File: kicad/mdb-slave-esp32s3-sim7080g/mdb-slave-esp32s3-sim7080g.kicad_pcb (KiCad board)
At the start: 2 copper layers, 65 x 40 mm, 69 parts, among them J1 USB_C_Receptacle_USB2.0_16P, J2 JAE_SIM_Card_SF72S006, J3 Conn_02x11_Odd_Even, J4 Conn_Coaxial, J5 Conn_Coaxial, J6 MDB_Connector, Q1 NPN, Q2 NPN, Q3 NPN, SW1 SW_Push, U1 ESP32-S3FH4R2, U2 SIM7080G, U3 LM2594HVM-3.3, U4 TLP785, U5 TLP785, Y1 Crystal_GND24

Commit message: Updating routes
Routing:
- net GND: track 425.9 -> 426.8 mm
- net /mdb_communications_common: track 30.1 -> 30.6 mm

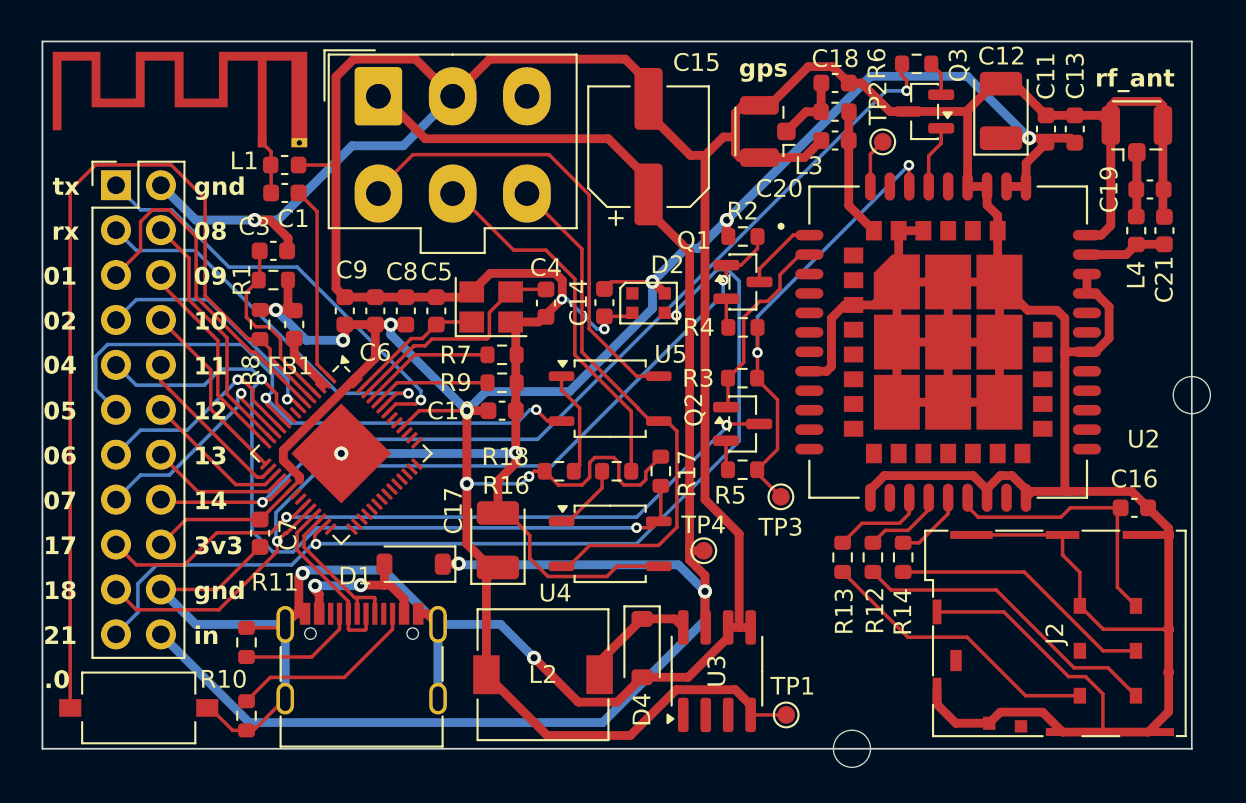
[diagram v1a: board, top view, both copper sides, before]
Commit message: Adding NTC thermal sensor
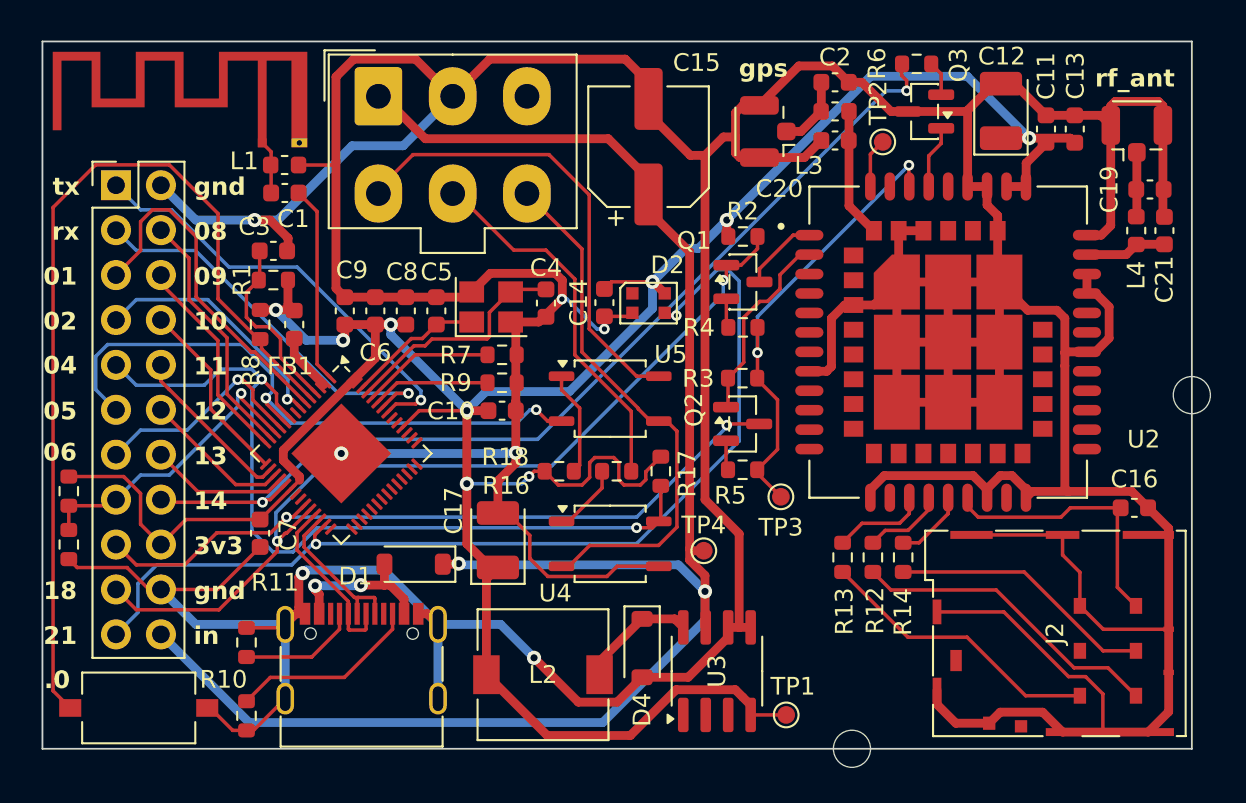
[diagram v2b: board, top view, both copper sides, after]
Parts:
- removed C18: 27pf, Capacitor_SMD:C_0603_1608Metric
- added C2: 1.8pf, Capacitor_SMD:C_0603_1608Metric, F.Cu at (213.3, 85.4)
- added R15: 10k, Resistor_SMD:R_0603_1608Metric, F.Cu at (170.0, 108.5)
- added TH1: Thermistor_NTC, Resistor_SMD:R_0603_1608Metric, F.Cu at (170.0, 111.5)
- C19: value 27pf -> 1.8pf
- L3: value 47nh -> 5.6nh
- L4: value 47nh -> 3.9nh
- R2, R3: value 10K -> 10k
- moved REF** 2.96 mm to (220.8, 111.5)
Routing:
- net +3V3: track 152.4 -> 160.3 mm
- net GND: track 426.8 -> 432.8 mm
- net /io7: track 12.9 -> 17.1 mm

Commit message: Updating LED footprint
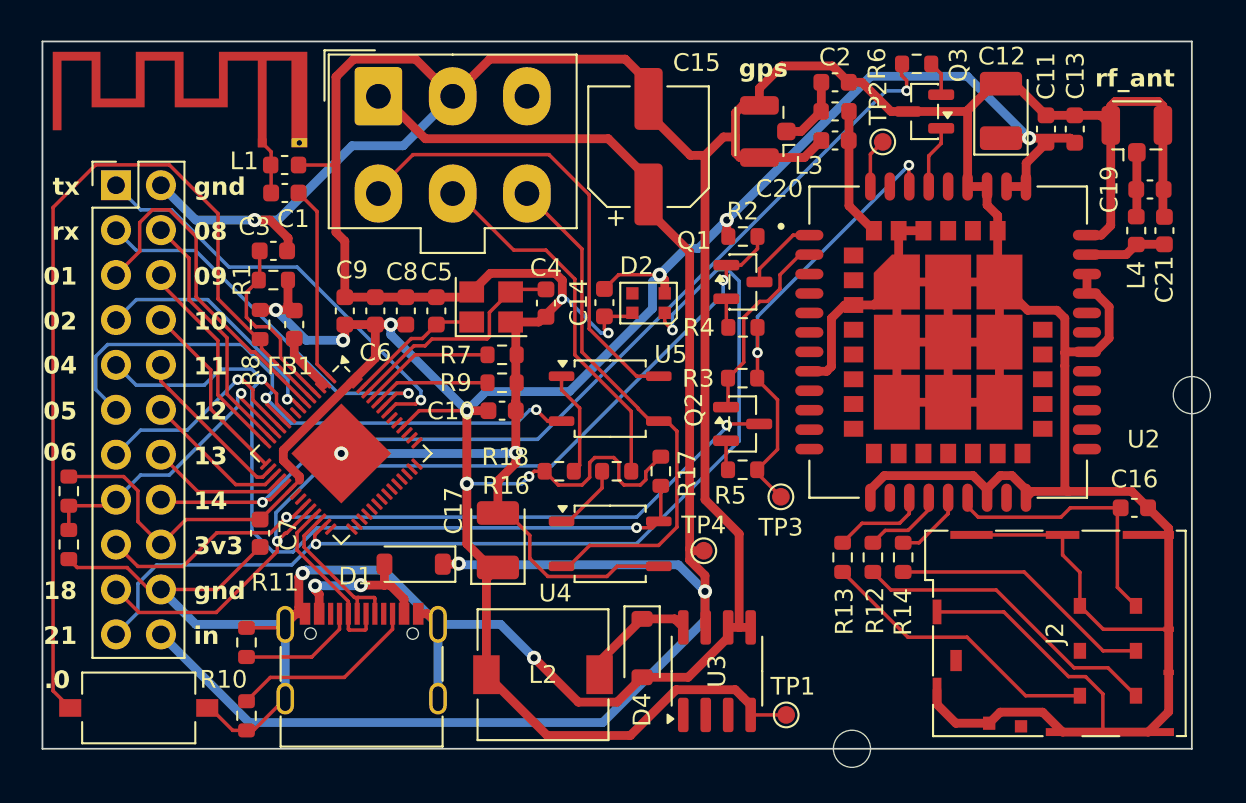
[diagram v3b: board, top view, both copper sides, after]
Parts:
- moved REF** 5.61 mm to (221.5, 106.0)
- turned D2 to 180 degrees
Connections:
- D2 pad 1: unconnected-(D2-DOUT-Pad1) -> /io21
- D2 pad 2: GND -> +3V3
- D2 pad 3: /io21 -> unconnected-(D2-DOUT-Pad3)
- D2 pad 4: +3V3 -> GND
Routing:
- net /io21: track 57.0 -> 58.3 mm
- net GND: track 432.8 -> 434.0 mm
- net +3V3: track 160.3 -> 161.1 mm

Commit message: Updating sim7080g transistors
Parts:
- removed REF**: OSHW-Logo2_14.6x12mm_SilkScreen, Symbol:OSHW-Logo2_14.6x12mm_SilkScreen
- Q1, Q2, Q3: value NPN -> MMBT3904
- moved Q2 21.4 mm to (218.5, 86.1), turned to 180 degrees
- moved Q3 14.1 mm to (208.1, 96.7)
- moved Q1 8.09 mm to (208.1, 104.8), turned to 180 degrees
- moved R6 4.54 mm to (218.9, 88.8)
- moved TP2 0.89 mm to (216.0, 87.9)
- moved R4 0.12 mm to (208.1, 99.4)
- moved C20 0.10 mm to (213.3, 88.8)
- moved L3 0.05 mm to (213.3, 87.1)
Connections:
- Q1 pad 1: /io18 -> Net-(Q1-B)
- Q1 pad 2: Net-(Q1-B) -> /io17
- Q1 pad 3: /sim_uart1_tx -> /sim_uart1_rx
- Q2 pad 1: /sim_uart1_rx -> Net-(Q2-B)
- Q2 pad 2: Net-(Q2-B) -> GND
- Q2 pad 3: /io17 -> /pwrkey
- Q3 pad 1: /pwrkey -> Net-(Q3-B)
- Q3 pad 2: Net-(Q3-B) -> /sim_uart1_tx
- Q3 pad 3: GND -> /io18
- R4 pad 2: Net-(Q1-B) -> Net-(Q3-B)
- R5 pad 2: Net-(Q2-B) -> Net-(Q1-B)
- R6 pad 1: Net-(Q3-B) -> Net-(Q2-B)
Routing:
- net /pwrkey: track 3.58 -> 5.76 mm
- net /io14: track 55.3 -> 53.1 mm
- net /sim_uart1_rx: track 11.1 -> 12.6 mm
- net Net-(Q1-B): track 1.67 -> 2.79 mm
- net Net-(Q3-B): track 1.97 -> 3.00 mm
- net Net-(U2-STATUS): track 2.81 -> 3.70 mm
- net /io17: track 41.7 -> 42.3 mm
- net /io18: track 51.0 -> 50.4 mm
- net /sim_uart1_tx: track 4.35 -> 3.76 mm

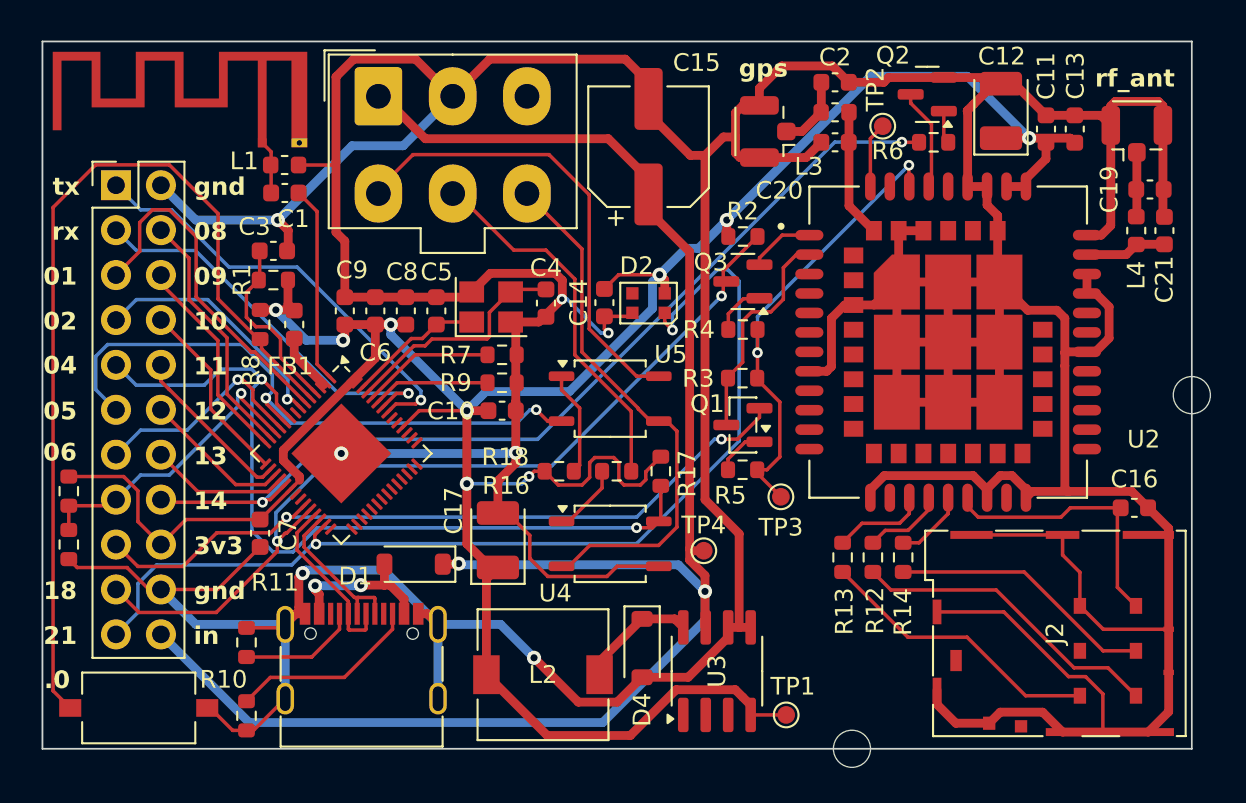
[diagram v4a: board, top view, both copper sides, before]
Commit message: Adding buzzer and DEX level shifter
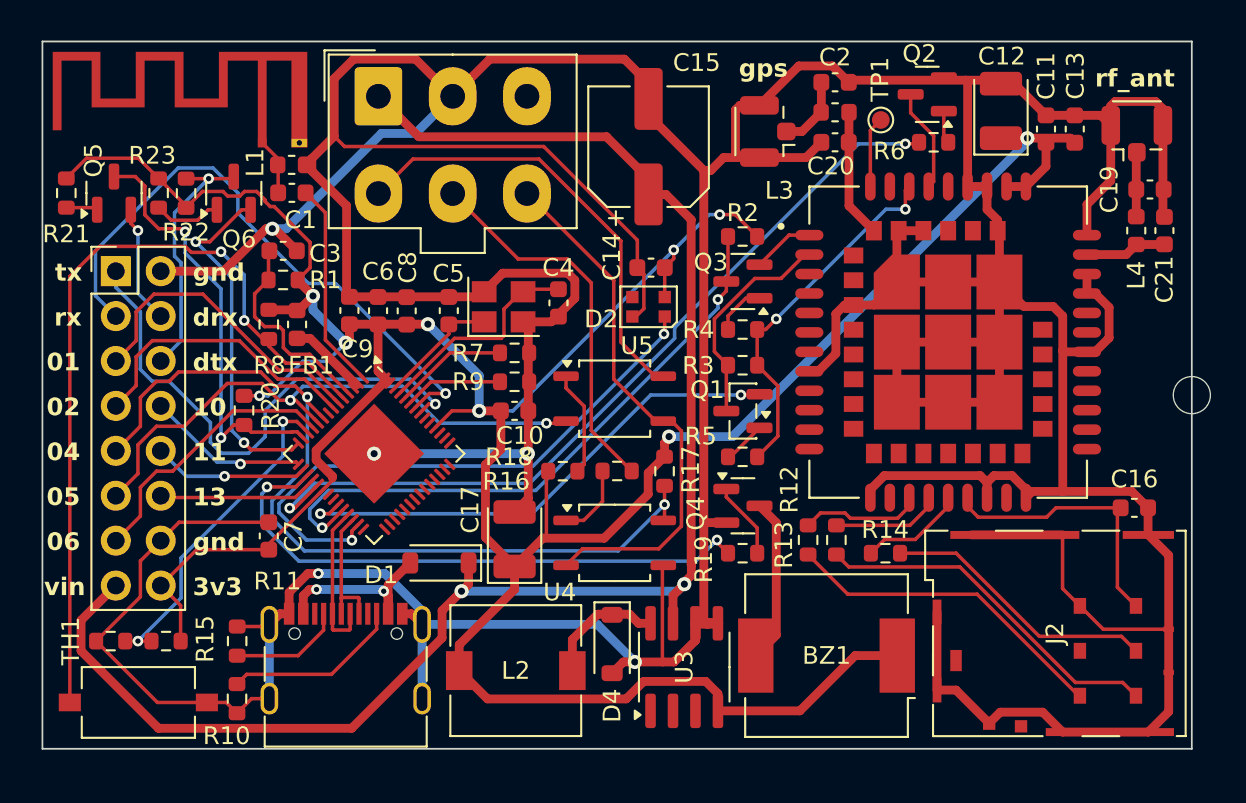
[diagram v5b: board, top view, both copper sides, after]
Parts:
- removed H2: MountingHole, MountingHole:MountingHole_2.1mm
- removed J3: Conn_02x11_Odd_Even, Connector_PinHeader_2.54mm:PinHeader_2x11_P2.54mm_Vertical
- removed TP2, TP3, TP4: TestPoint, TestPoint:TestPoint_Pad_D1.0mm
- added BZ1: Buzzer, Buzzer_Beeper:Buzzer_CUI_CPT-9019S-SMT, F.Cu at (212.8, 117.8)
- added J7: Conn_02x08_Odd_Even, Connector_PinHeader_2.54mm:PinHeader_2x08_P2.54mm_Vertical, F.Cu at (172.7, 96.1)
- added Q4: MMBT3904, Package_TO_SOT_SMD:SOT-23, F.Cu at (208.1, 109.3)
- added Q5: MMBT3904, Package_TO_SOT_SMD:SOT-23, F.Cu at (172.5, 91.7)
- added Q6: MMBT3904, Package_TO_SOT_SMD:SOT-23, F.Cu at (179.3, 91.7)
- added R19: 4K7, Resistor_SMD:R_0603_1608Metric, F.Cu at (208.1, 112.0)
- added R20: 10k, Resistor_SMD:R_0603_1608Metric, F.Cu at (179.9, 104.0)
- added R21: 4K7, Resistor_SMD:R_0603_1608Metric, F.Cu at (169.8, 91.7)
- added R22: 10k, Resistor_SMD:R_0603_1608Metric, F.Cu at (176.6, 91.7)
- added R23: 4K7, Resistor_SMD:R_0603_1608Metric, F.Cu at (175.1, 91.7)
- added REF**: OSHW-Logo_11.4x12mm_SilkScreen, Symbol:OSHW-Logo_11.4x12mm_SilkScreen, B.Cu at (220.7, 104.4)
- moved TP1 34.1 mm to (215.9, 87.5)
- moved H1 27.7 mm to (233.5, 103.1)
- moved R15 10.1 mm to (175.5, 117.0), turned to 0 degrees
- moved TH1 5.95 mm to (172.4, 117.0), turned to 0 degrees
- moved C14 3.30 mm to (202.9, 95.9), turned to 0 degrees
- moved R12 2.29 mm to (213.4, 111.3)
- moved R13 2.18 mm to (211.8, 111.3)
- moved U3 1.86 mm to (204.8, 118.5)
- moved U1 1.85 mm to (187.3, 106.4)
- moved D4 1.71 mm to (200.7, 117.2)
- moved L2 1.56 mm to (195.3, 118.7)
- moved D1 1.46 mm to (190.9, 112.6)
- moved R10 1.11 mm to (179.5, 120.3)
- moved R14 1.03 mm to (216.2, 112.0), turned to 0 degrees
- moved C17 0.94 mm to (195.2, 111.2)
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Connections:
- C10 pad 1: GND -> +3V3
- C10 pad 2: +3V3 -> GND
- C9 pad 1: GND -> +3V3
- C9 pad 2: +3V3 -> GND
- TP1 pad 1: +3V3 -> Net-(U2-STATUS)
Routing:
- net +3V3: track 161.1 -> 199.1 mm
- net /io21: track 58.3 -> 33.1 mm
- net /io12: track 8.49 -> 33.0 mm, vias 0 -> 2
- net /io18: track 50.4 -> 35.2 mm
- net /dex_tx: track 0.00 -> 14.5 mm, vias 0 -> 1
- net /io17: track 42.3 -> 28.9 mm
- net GND: track 434.4 -> 422.0 mm, vias 7 -> 5
- net /u0rxd: track 22.2 -> 33.9 mm
- net /io8: track 14.3 -> 24.0 mm, vias 0 -> 2
- net Net-(BZ1--): track 0.00 -> 9.34 mm
- net /io9: track 11.9 -> 19.7 mm, vias 0 -> 2
- net /boot: track 52.8 -> 45.6 mm, vias 0 -> 2
- net /dex_rx: track 0.00 -> 6.72 mm, vias 0 -> 1
- net /io14: track 53.1 -> 46.7 mm
- net /vin: track 97.2 -> 90.8 mm
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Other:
- board text added: "drx"
- board text added: "dtx"
- board text added: "vin"
- board text removed: ".0"
- board text removed: "07"
- board text removed: "08"
- board text removed: "09"
- board text removed: "12"
- board text removed: "14"
- board text removed: "17"
- board text removed: "18"
- board text removed: "21"
- board text removed: "in"

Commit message: routing..
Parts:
- removed REF**: OSHW-Logo_11.4x12mm_SilkScreen, Symbol:OSHW-Logo_11.4x12mm_SilkScreen
- added J3: Conn_01x03_Pin, Connector_JST:JST_PH_B3B-PH-K_1x03_P2.00mm_Vertical, F.Cu at (175.9, 93.1)
- added J8: Conn_01x04_Pin, Connector_JST:JST_PH_B4B-PH-K_1x04_P2.00mm_Vertical, F.Cu at (177.9, 103.5)
- added Q7: MMBT3904, Package_TO_SOT_SMD:SOT-23, F.Cu at (172.4, 115.9)
- added R24: 4K7, Resistor_SMD:R_0603_1608Metric, F.Cu at (174.1, 106.9)
- added R25: 4K7, Resistor_SMD:R_0603_1608Metric, F.Cu at (171.0, 106.9)
- added R27: 4K7, Resistor_SMD:R_0603_1608Metric, F.Cu at (175.4, 115.9)
- J7: value Conn_02x08_Odd_Even -> Conn_01x03_Pin; footprint Connector_PinHeader_2.54mm:PinHeader_2x08_P2.54mm_Vertical -> Connector_JST:JST_PH_B3B-PH-K_1x03_P2.00mm_Vertical
- moved J7 15.8 mm to (175.9, 111.5), turned to 180 degrees
- moved R21 12.2 mm to (180.1, 98.3)
- moved Q6 10.6 mm to (170.6, 97.7)
- moved R15 9.02 mm to (179.5, 108.9), turned to 90 degrees
- moved TH1 8.59 mm to (179.5, 112.2), turned to 90 degrees
- moved Q5 7.92 mm to (177.5, 97.8)
- moved R23 6.88 mm to (173.2, 98.3)
- moved R22 6.86 mm to (174.8, 98.3)
- moved R20 1.74 mm to (181.6, 103.7)
- moved C7 1.23 mm to (181.6, 112.2)
- moved C9 1.01 mm to (184.8, 98.3)
- moved C3 0.93 mm to (182.5, 94.1)
- moved R1 0.93 mm to (182.5, 95.7)
- moved R8 0.86 mm to (181.7, 98.3)
- moved FB1 0.86 mm to (183.3, 98.3)
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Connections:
- J7 pad 1: /u0txd -> GND
- J7 pad 2: GND -> /vin
- J7 pad 3: /u0rxd -> Net-(J7-Pin_3)
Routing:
- net GND: track 422.0 -> 0.00 mm, vias 5 -> 0
- net +3V3: track 199.1 -> 0.00 mm, vias 9 -> 0
- net /vin: track 90.8 -> 0.00 mm, vias 2 -> 0
- net /io4: track 49.5 -> 0.00 mm, vias 2 -> 0
- net /io14: track 46.7 -> 0.00 mm, vias 2 -> 0
- net /boot: track 45.6 -> 0.00 mm, vias 2 -> 0
- net /io18: track 35.2 -> 0.00 mm, vias 2 -> 0
- net /u0rxd: track 33.9 -> 0.00 mm, vias 1 -> 0
- net /io21: track 33.1 -> 0.00 mm, vias 2 -> 0
- net /io12: track 33.0 -> 0.00 mm, vias 2 -> 0
- net /io5: track 32.8 -> 0.00 mm, vias 2 -> 0
- net /mdb_communications_common: track 30.4 -> 0.00 mm
- net /u0txd: track 29.7 -> 0.00 mm, vias 1 -> 0
- net /io17: track 28.9 -> 0.00 mm, vias 2 -> 0
- net /mdb_master_receive: track 25.4 -> 0.00 mm
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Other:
- board text removed: "01"
- board text removed: "02"
- board text removed: "04"
- board text removed: "05"
- board text removed: "06"
- board text removed: "10"
- board text removed: "11"
- board text removed: "13"
- board text removed: "3v3"
- board text removed: "drx"
- board text removed: "dtx"
- board text removed: "gnd"
- board text removed: "rx"
- board text removed: "tx"
- board text removed: "vin"

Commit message: routing...
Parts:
- moved C8 0.30 mm to (189.4, 98.3)
- moved C6 0.30 mm to (187.8, 98.3)
- moved R7 0.14 mm to (195.2, 100.8)
- moved Q5 0.11 mm to (177.4, 97.8), turned to -90 degrees
- moved R9 0.07 mm to (195.2, 102.4)
- moved Q6 0.06 mm to (170.7, 97.7)
- moved C9 0.06 mm to (184.9, 98.3)
- moved FB1 0.06 mm to (183.3, 98.3)
- moved R21 0.06 mm to (180.1, 98.3)
- moved R22 0.06 mm to (174.8, 98.3)
- moved R23 0.06 mm to (173.3, 98.3), turned to 90 degrees
- moved R8 0.06 mm to (181.7, 98.3)
- turned C7 to 90 degrees
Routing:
- net /boot: track 0.00 -> 51.3 mm
- net +3V3: track 0.00 -> 50.4 mm
- net GND: track 0.00 -> 46.2 mm, vias 0 -> 1
- net /io11: track 0.00 -> 19.0 mm
- net /io9: track 0.00 -> 15.5 mm
- net Net-(U1-CHIP_PU/RESET): track 0.00 -> 14.4 mm
- net /io10: track 0.00 -> 14.2 mm
- net /io13: track 0.00 -> 12.0 mm
- net Net-(U1-XTAL_N): track 0.00 -> 12.0 mm
- net Net-(J1-CC2): track 0.00 -> 10.0 mm
- net /dex_tx: track 0.00 -> 9.81 mm
- net /io8: track 0.00 -> 9.71 mm
- net /usb-: track 0.00 -> 9.09 mm
- net /usb+: track 0.00 -> 8.71 mm
- net Net-(D1-A): track 0.00 -> 7.41 mm, vias 0 -> 2
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
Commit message: routing...
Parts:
- added REF**: OSHW-Logo_11.4x12mm_SilkScreen, Symbol:OSHW-Logo_11.4x12mm_SilkScreen, B.Cu at (210.5, 109.1)
- moved C11 0.40 mm to (224.9, 88.0)
- moved C12 0.40 mm to (222.3, 87.0)
- moved C13 0.40 mm to (226.5, 88.0)
- turned R18 to 180 degrees
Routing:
- net GND: track 46.2 -> 427.7 mm, vias 1 -> 4
- net +3V3: track 50.4 -> 208.1 mm, vias 0 -> 9
- net /vin: track 0.00 -> 80.6 mm, vias 0 -> 2
- net /io14: track 3.07 -> 53.0 mm, vias 1 -> 2
- net /io18: track 1.97 -> 39.8 mm, vias 1 -> 2
- net /io21: track 1.51 -> 38.6 mm, vias 1 -> 2
- net /io12: track 3.36 -> 32.7 mm, vias 1 -> 2
- net /mdb_communications_common: track 0.00 -> 27.7 mm
- net /io17: track 1.87 -> 29.5 mm, vias 1 -> 2
- net /mdb_master_receive: track 0.00 -> 25.3 mm
- net /io4: track 2.21 -> 25.2 mm, vias 1 -> 2
- net /mdb_master_transmit: track 0.00 -> 21.5 mm
- net /sim_vdd_ext: track 0.00 -> 20.5 mm, vias 0 -> 2
- net Net-(J2-CLK): track 0.00 -> 20.2 mm
- net Net-(J2-I/O): track 0.00 -> 18.7 mm
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- added copper zone on F.Cu, net +3V3
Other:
- board text added: "3v3"
- board text added: "DEX"
- board text added: "D_RX"
- board text added: "D_TX"
- board text added: "GND"
- board text added: "PULSE"
- board text added: "SCL"
- board text added: "SDA"
- board text added: "VIN"
- board text added: "_i2c"
